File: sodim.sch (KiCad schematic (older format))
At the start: 1 part, among them J1 ddr4-sodimm-edge-connector

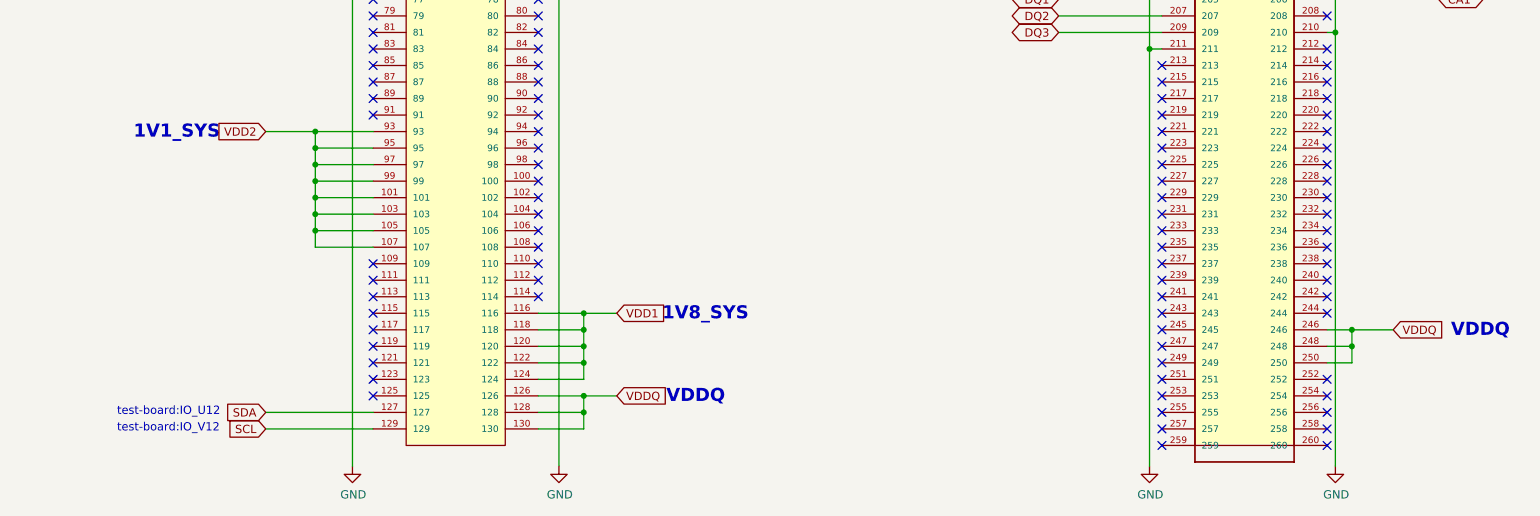
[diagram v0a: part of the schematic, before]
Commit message: Fix power labels naming scheme, remove connection from SODIM to VDDQ, add chockes to DDR5 power
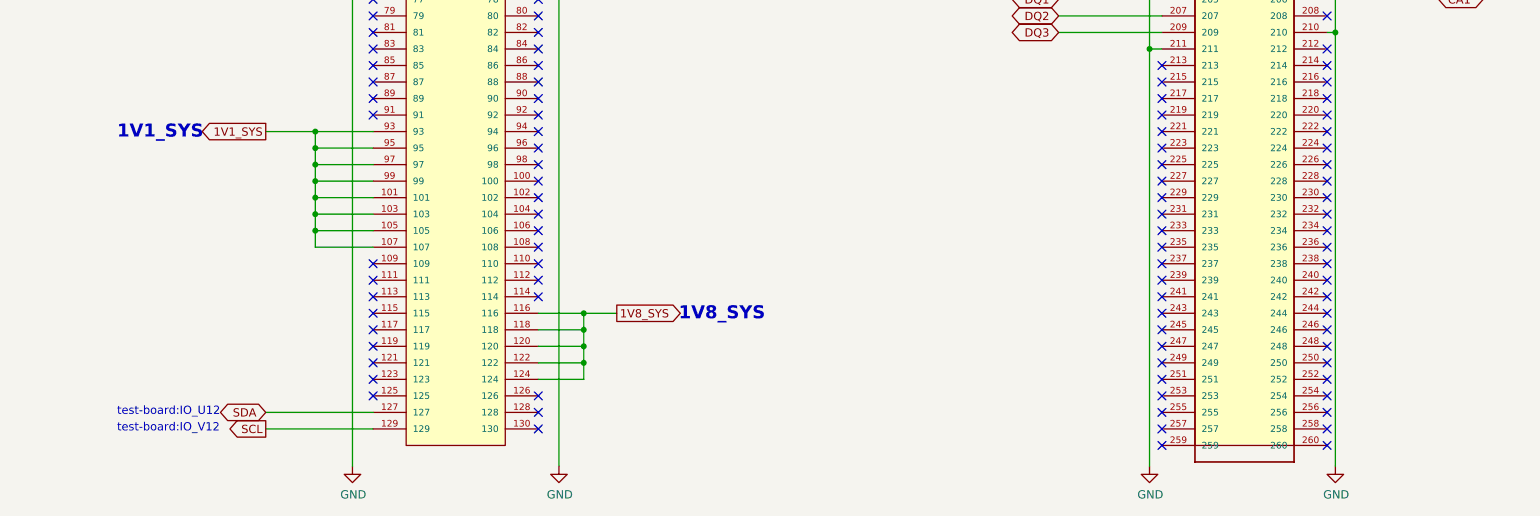
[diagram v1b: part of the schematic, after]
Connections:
- net VDD1 renamed 1V8_SYS
- net VDD2 renamed 1V1_SYS
- removed net VDDQ: J1.126, J1.128, J1.130, J1.246, J1.248, J1.250
- no-connect marks 143 -> 149
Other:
- note removed: "VDDQ"
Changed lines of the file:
@@
 	4375 7100 4075 7100
 Connection ~ 4375 7100
-Text GLabel 4075 7100 0    50   Input ~ 0
-VDD2
-Text Notes 3275 7150 0    79   ~ 16
+Text GLabel 4075 7100 0    50   Output ~ 0
+1V1_SYS
+Text Notes 3175 7150 0    79   ~ 16
 1V1_SYS
 Wire Wire Line
@@
 	6000 8600 6000 8500
 Connection ~ 6000 8500
-Text GLabel 6200 8200 2    50   Input ~ 0
-VDD1
-Text Notes 6475 8250 0    79   ~ 16
+Text GLabel 6200 8200 2    50   Output ~ 0
+1V8_SYS
+Text Notes 6575 8250 0    79   ~ 16
 1V8_SYS
-Wire Wire Line
-	5725 8700 6000 8700
-Wire Wire Line
-	5725 8800 6000 8800
-Wire Wire Line
-	6000 8800 6000 8700
-Connection ~ 6000 8700
-Wire Wire Line
-	6000 8700 6200 8700
-Wire Wire Line
-	5725 8900 6000 8900
-Wire Wire Line
-	6000 8900 6000 8800
-Connection ~ 6000 8800
-Text GLabel 6200 8700 2    50   Input ~ 0
-VDDQ
-Text Notes 6500 8750 0    79   ~ 16
-VDDQ
-Text Notes 11250 8350 0    79   ~ 16
-VDDQ
-Wire Wire Line
-	10500 8300 10650 8300
-Text GLabel 10900 8300 2    50   Input ~ 0
-VDDQ
-Wire Wire Line
-	10500 8400 10650 8400
-Wire Wire Line
-	10650 8400 10650 8300
-Connection ~ 10650 8300
-Wire Wire Line
-	10650 8300 10900 8300
-Wire Wire Line
-	10500 8500 10650 8500
-Wire Wire Line
-	10650 8500 10650 8400
-Connection ~ 10650 8400
 Wire Wire Line
 	10500 3700 10550 3700
@@
 IO_N5
 NoConn ~ 10500 6100
-Text GLabel 4075 8800 0    50   Input ~ 0
+Text GLabel 4075 8800 0    50   BiDi ~ 0
 SDA
-Text GLabel 4075 8900 0    50   Input ~ 0
+Text GLabel 4075 8900 0    50   Output ~ 0
 SCL
 Text Notes 3175 8825 0    50   ~ 0
@@
 EndData
 $EndBitmap
+NoConn ~ 5725 8700
+NoConn ~ 5725 8800
+NoConn ~ 5725 8900
+NoConn ~ 10500 8300
+NoConn ~ 10500 8400
+NoConn ~ 10500 8500
 $EndSCHEMATC
